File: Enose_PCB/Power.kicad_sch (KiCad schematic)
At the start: 53 parts, among them IC1 ISL91127IRNZ-T7A, J5 USB_C_Receptacle_USB2.0_16P, J6 Battery Terminal, SW3 SW_DPST_x2, U2 USBLC6-2P6, U3 MP2721GRH-0000-P

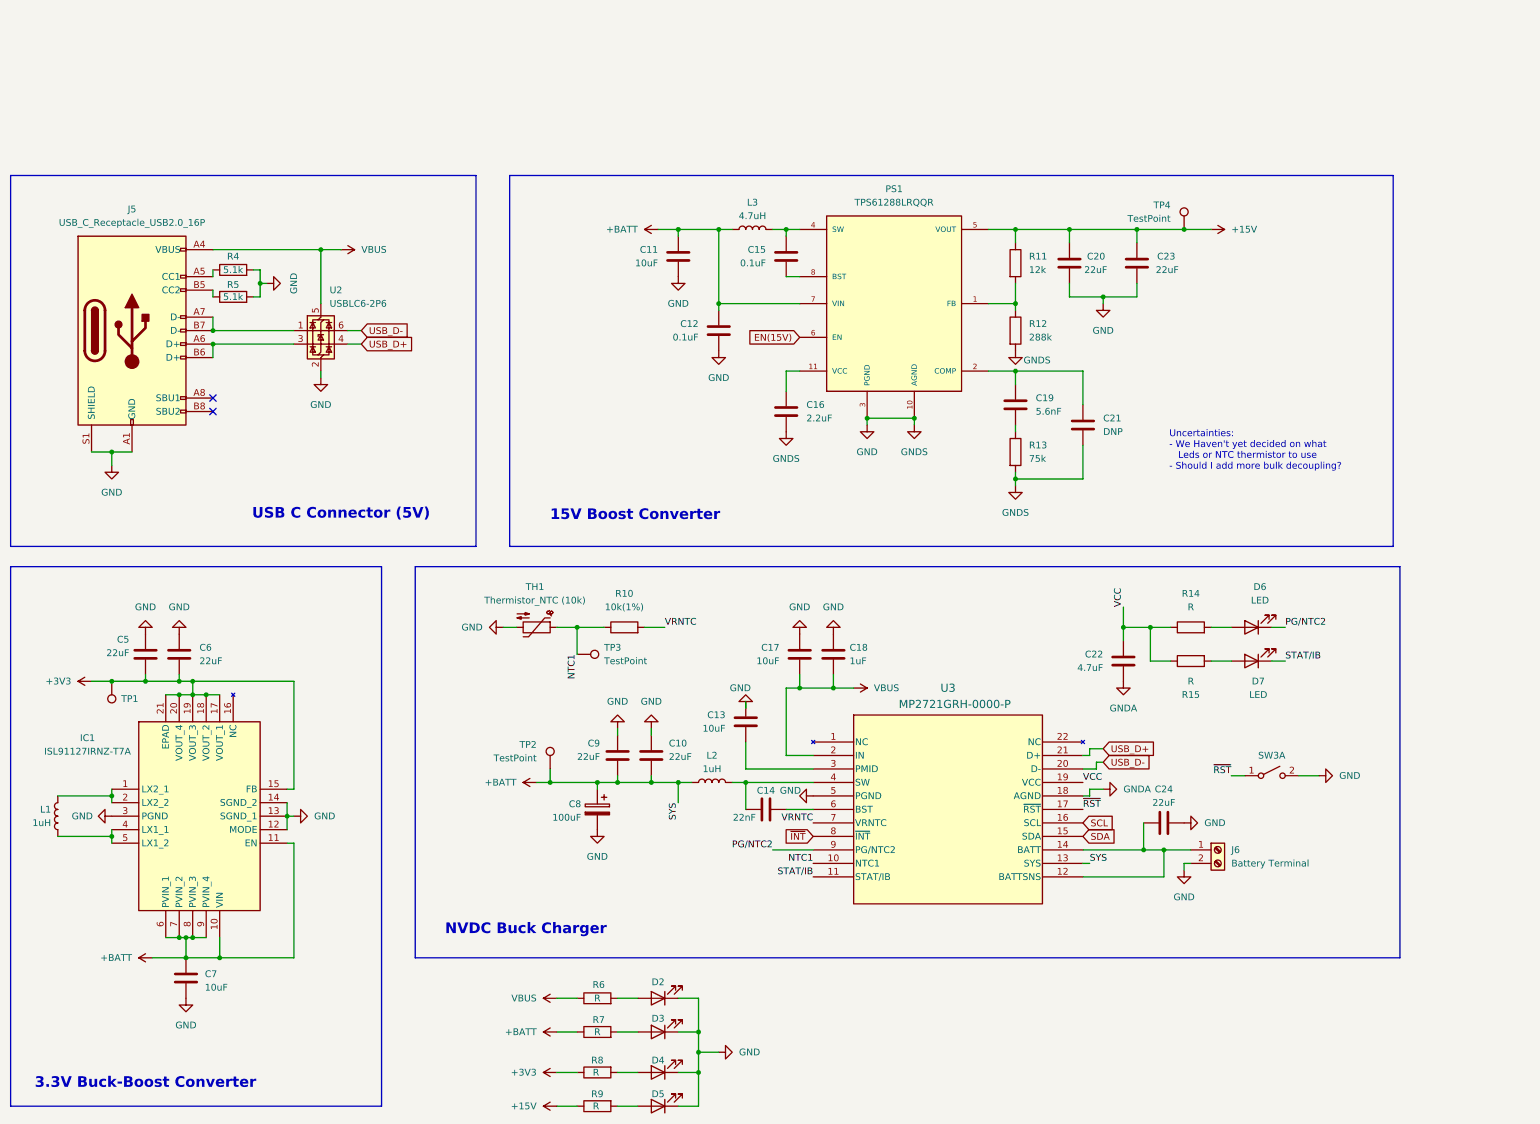
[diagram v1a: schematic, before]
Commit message: Added LED
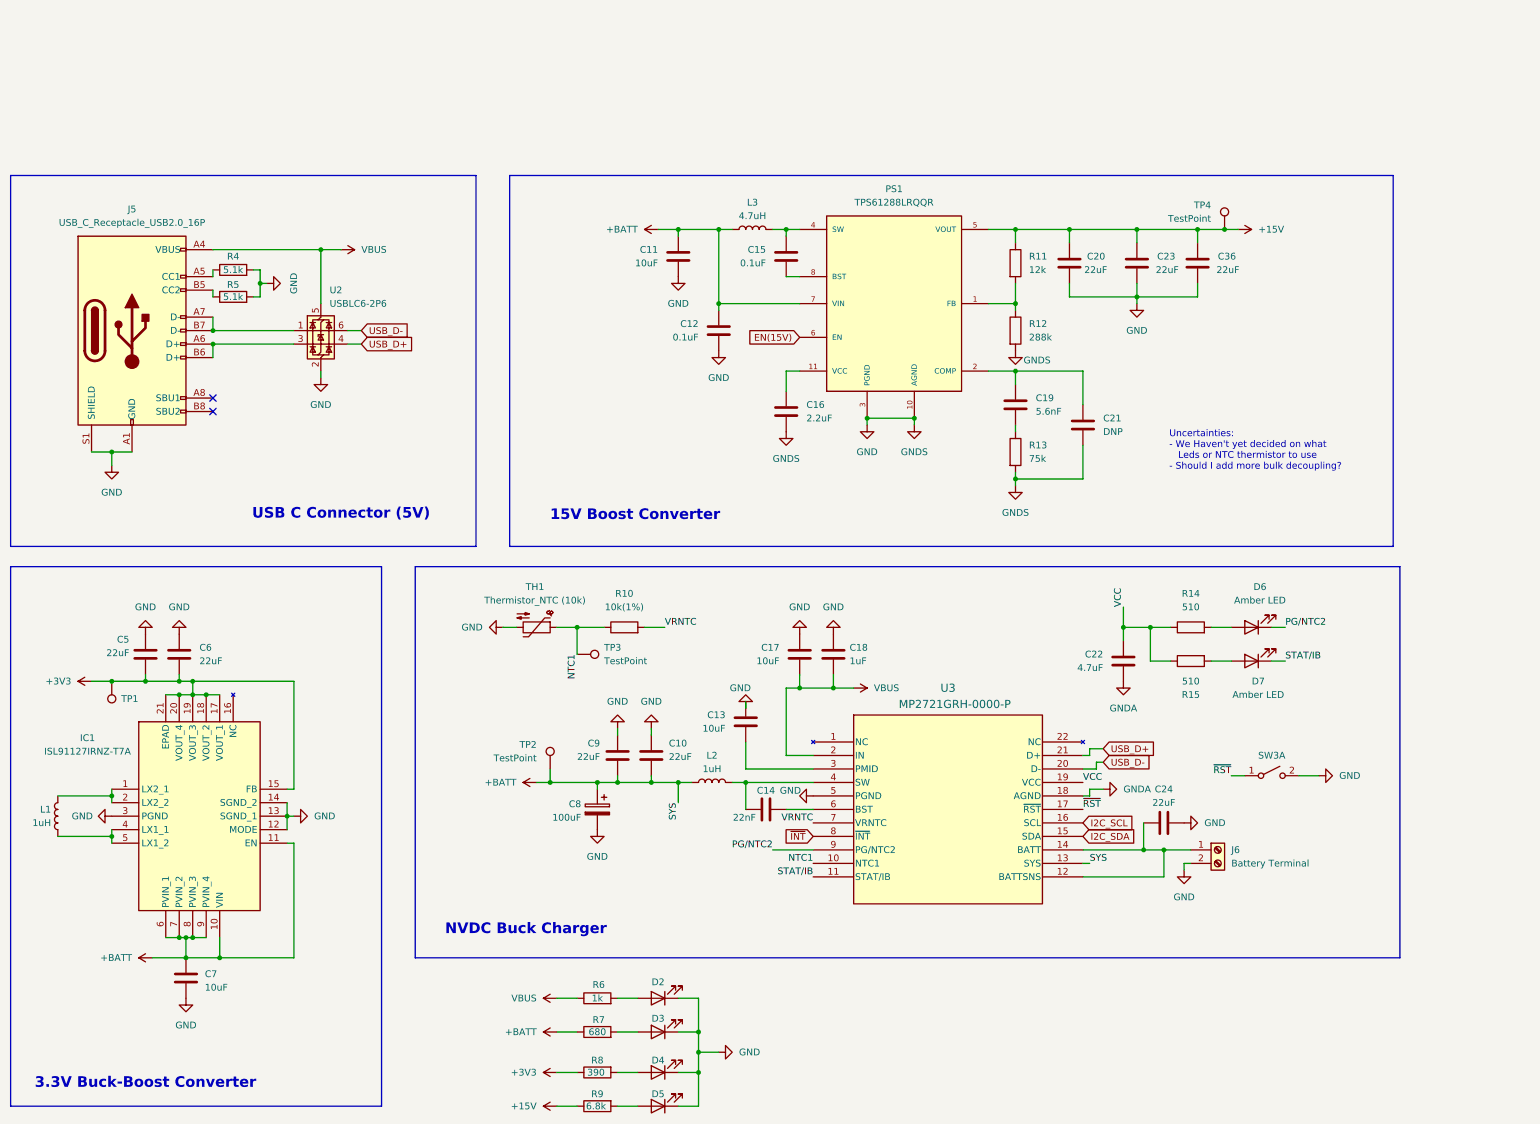
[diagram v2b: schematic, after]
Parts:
- added C36: 22uF, Capacitor_THT:C_Disc_D6.0mm_W4.4mm_P5.00mm, symbol Device:C
- C20, C23: footprint (none) -> Capacitor_SMD:C_1210_3225Metric
- D4, D5: value LED -> LED GREEN
- D6, D7: value LED -> Amber LED
- R14, R15: value R -> 510
- R6: value R -> 1k
- R7: value R -> 680
- R8: value R -> 390
- R9: value R -> 6.8k
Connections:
- net +15V: now also C36.1
- net GND: now also C36.2
- net SCL renamed I2C_SCL
- net SDA renamed I2C_SDA
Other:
- moved on the sheet: TP4
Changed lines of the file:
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@@
 	)
 	(junction
+		(at 248.92 25.4)
+		(diameter 0)
+		(color 0 0 0 0)
+	)
+	(junction
 		(at 149.86 180.34)
 		(diameter 0)
@@
 	)
 	(junction
+		(at 232.41 38.1)
+		(diameter 0)
+		(color 0 0 0 0)
+	)
+	(junction
 		(at 229.87 100.33)
 		(diameter 0)
@@
 	)
 	(junction
-		(at 241.3 25.4)
-		(diameter 0)
-		(color 0 0 0 0)
-	)
-	(junction
 		(at 67.31 35.56)
 		(diameter 0)
@@
 	)
 	(junction
+		(at 243.84 25.4)
+		(diameter 0)
+		(color 0 0 0 0)
+	)
+	(junction
 		(at 209.55 72.39)
 		(diameter 0)
@@
 	)
 	(junction
-		(at 226.06 38.1)
-		(diameter 0)
-		(color 0 0 0 0)
-	)
-	(junction
 		(at 58.42 44.45)
 		(diameter 0)
@@
 	(wire
 		(pts
+			(xy 243.84 25.4) (xy 243.84 27.94)
+		)
+		(stroke
+			(width 0)
+			(type default)
+		)
+	)
+	(wire
+		(pts
 			(xy 58.42 29.21) (xy 78.74 29.21)
 		)
@@
 	(wire
 		(pts
-			(xy 232.41 25.4) (xy 241.3 25.4)
+			(xy 232.41 25.4) (xy 243.84 25.4)
 		)
 		(stroke
@@
 	(wire
 		(pts
-			(xy 219.71 38.1) (xy 226.06 38.1)
+			(xy 219.71 38.1) (xy 232.41 38.1)
 		)
 		(stroke
@@
 	(wire
 		(pts
-			(xy 241.3 25.4) (xy 246.38 25.4)
-		)
-		(stroke
-			(width 0)
-			(type default)
-		)
-	)
-	(wire
-		(pts
 			(xy 123.19 170.18) (xy 127 170.18)
 		)
@@
 	(wire
 		(pts
-			(xy 226.06 38.1) (xy 232.41 38.1)
-		)
-		(stroke
-			(width 0)
-			(type default)
-		)
-	)
-	(wire
-		(pts
 			(xy 262.89 128.27) (xy 266.7 128.27)
 		)
@@
 	(wire
 		(pts
-			(xy 226.06 38.1) (xy 226.06 39.37)
+			(xy 232.41 38.1) (xy 232.41 39.37)
 		)
 		(stroke
@@
 	(wire
 		(pts
+			(xy 243.84 38.1) (xy 232.41 38.1)
+		)
+		(stroke
+			(width 0)
+			(type default)
+		)
+	)
+	(wire
+		(pts
 			(xy 229.87 100.33) (xy 234.95 100.33)
 		)
@@
 	(wire
 		(pts
+			(xy 243.84 35.56) (xy 243.84 38.1)
+		)
+		(stroke
+			(width 0)
+			(type default)
+		)
+	)
+	(wire
+		(pts
 			(xy 123.19 176.53) (xy 127 176.53)
 		)
@@
 	(wire
 		(pts
+			(xy 243.84 25.4) (xy 248.92 25.4)
+		)
+		(stroke
+			(width 0)
+			(type default)
+		)
+	)
+	(wire
+		(pts
 			(xy 222.25 147.32) (xy 237.49 147.32)
 		)
@@
 	(wire
 		(pts
+			(xy 248.92 25.4) (xy 251.46 25.4)
+		)
+		(stroke
+			(width 0)
+			(type default)
+		)
+	)
+	(wire
+		(pts
 			(xy 223.52 132.08) (xy 222.25 132.08)
 		)
@@
 		)
 	)
-	(global_label "SDA"
+	(global_label "I2C_SDA"
 		(shape input)
 		(at 222.25 139.7 0)
@@
 		)
 		(property "Intersheetrefs" "${INTERSHEET_REFS}"
-			(at 228.8033 139.7 0)
+			(at 232.8552 139.7 0)
 			(effects
 				(font
@@
 		)
 	)
-	(global_label "SCL"
+	(global_label "I2C_SCL"
 		(shape input)
 		(at 222.25 137.16 0)
@@
 		)
 		(property "Intersheetrefs" "${INTERSHEET_REFS}"
-			(at 228.7428 137.16 0)
+			(at 232.7947 137.16 0)
 			(effects
 				(font
@@
 			)
 		)
-		(property "Value" "LED"
+		(property "Value" "Amber LED"
 			(at 255.27 113.03 0)
 			(effects
@@
 			)
 		)
-		(property "Value" "R"
+		(property "Value" "1k"
 			(at 130.81 170.18 90)
 			(effects
@@
 			)
 		)
-		(property "Value" "LED"
+		(property "Value" "Amber LED"
 			(at 255.5875 95.25 0)
 			(effects
@@
 			)
 		)
-		(property "Value" "LED"
+		(property "Value" "LED GREEN"
 			(at 143.764 189.738 0)
 			(effects
@@
 			)
 		)
-		(property "Footprint" ""
+		(property "Footprint" "Capacitor_SMD:C_1210_3225Metric"
 			(at 220.6752 35.56 0)
 			(effects
@@
 	(symbol
 		(lib_id "power:+15V")
-		(at 246.38 25.4 270)
+		(at 251.46 25.4 270)
 		(unit 1)
 		(exclude_from_sim no)
@@
 		(fields_autoplaced yes)
 		(property "Reference" "#PWR031"
-			(at 242.57 25.4 0)
+			(at 247.65 25.4 0)
 			(effects
 				(font
@@
 		)
 		(property "Value" "+15V"
-			(at 250.19 25.3999 90)
+			(at 255.27 25.3999 90)
 			(effects
 				(font
@@
 		)
 		(property "Footprint" ""
-			(at 246.38 25.4 0)
+			(at 251.46 25.4 0)
 			(effects
 				(font
@@
 		)
 		(property "Datasheet" ""
-			(at 246.38 25.4 0)
+			(at 251.46 25.4 0)
 			(effects
 				(font
@@
 		)
 		(property "Description" "Power symbol creates a global label with name \"+15V\""
-			(at 246.38 25.4 0)
+			(at 251.46 25.4 0)
 			(effects
 				(font
@@
 			)
 		)
-		(property "Value" "R"
+		(property "Value" "390"
 			(at 130.556 184.15 90)
 			(effects
@@
 			)
 		)
-		(property "Value" "R"
+		(property "Value" "510"
 			(at 242.57 96.52 90)
 			(effects
@@
 			)
 		)
-		(property "Value" "LED"
+		(property "Value" "LED GREEN"
 			(at 143.764 196.088 0)
 			(effects
@@
 			)
 		)
-		(property "Value" "R"
+		(property "Value" "6.8k"
 			(at 130.556 190.5 90)
 			(effects
@@
 			)
 		)
-		(property "Value" "R"
+		(property "Value" "510"
 			(at 242.57 110.49 90)
 			(effects
@@
 			)
 		)
-		(property "Value" "R"
+		(property "Value" "680"
 			(at 130.81 176.53 90)
 			(effects
@@
 	)
 	(symbol
+		(lib_id "Device:C")
+		(at 243.84 31.75 0)
+		(unit 1)
+		(exclude_from_sim no)
+		(in_bom yes)
+		(on_board yes)
+		(dnp no)
+		(property "Reference" "C36"
+			(at 247.65 30.4799 0)
+			(effects
+				(font
+					(size 1.27 1.27)
+				)
+				(justify left)
+			)
+		)
+		(property "Value" "22uF"
+			(at 247.396 33.02 0)
+			(effects
+				(font
+					(size 1.27 1.27)
+				)
+				(justify left)
+			)
+		)
+		(property "Footprint" "Capacitor_THT:C_Disc_D6.0mm_W4.4mm_P5.00mm"
+			(at 244.8052 35.56 0)
+			(effects
+				(font
+					(size 1.27 1.27)
+				)
+				(hide yes)
+			)
+		)
+		(property "Datasheet" "~"
+			(at 243.84 31.75 0)
+			(effects
+				(font
+					(size 1.27 1.27)
+				)
+				(hide yes)
+			)
+		)
+		(property "Description" "Unpolarized capacitor"
+			(at 243.84 31.75 0)
+			(effects
+				(font
+					(size 1.27 1.27)
+				)
+				(hide yes)
+			)
+		)
+		(pin "2"
+		)
+		(pin "1"
+		)
+		(instances
+			(project "Enose_PCB"
+				(path "/eef70be0-4107-491c-8ca0-465071a6397e/c704ca63-8ab0-46ce-942e-504221cfea41"
+					(reference "C36")
+					(unit 1)
+				)
+			)
+		)
+	)
+	(symbol
 		(lib_id "Device:R")
 		(at 209.55 44.45 0)
@@
 	(symbol
 		(lib_id "power:GND")
-		(at 226.06 39.37 0)
+		(at 232.41 39.37 0)
 		(unit 1)
 		(exclude_from_sim no)
@@
 		(fields_autoplaced yes)
 		(property "Reference" "#PWR029"
-			(at 226.06 45.72 0)
+			(at 232.41 45.72 0)
 			(effects
 				(font
@@
 		)
 		(property "Value" "GND"
-			(at 226.06 44.45 0)
+			(at 232.41 44.45 0)
 			(effects
 				(font
@@
 		)
 		(property "Footprint" ""
-			(at 226.06 39.37 0)
+			(at 232.41 39.37 0)
 			(effects
 				(font
@@
 		)
 		(property "Datasheet" ""
-			(at 226.06 39.37 0)
+			(at 232.41 39.37 0)
 			(effects
 				(font
@@
 		)
 		(property "Description" "Power symbol creates a global label with name \"GND\" , ground"
-			(at 226.06 39.37 0)
+			(at 232.41 39.37 0)
 			(effects
 				(font
@@
 	(symbol
 		(lib_id "Connector:TestPoint")
-		(at 241.3 25.4 0)
+		(at 248.92 25.4 0)
 		(mirror y)
 		(unit 1)
@@
 		(dnp no)
 		(property "Reference" "TP4"
-			(at 238.76 20.8279 0)
+			(at 246.38 20.8279 0)
 			(effects
 				(font
@@
 		)
 		(property "Value" "TestPoint"
-			(at 238.76 23.3679 0)
+			(at 246.38 23.3679 0)
 			(effects
 				(font
@@
 		)
 		(property "Footprint" ""
-			(at 236.22 25.4 0)
+			(at 243.84 25.4 0)
 			(effects
 				(font
@@
 		)
 		(property "Datasheet" "~"
-			(at 236.22 25.4 0)
+			(at 243.84 25.4 0)
 			(effects
 				(font
@@
 		)
 		(property "Description" "test point"
-			(at 241.3 25.4 0)
+			(at 248.92 25.4 0)
 			(effects
 				(font
@@
 			)
 		)
-		(property "Footprint" ""
+		(property "Footprint" "Capacitor_SMD:C_1210_3225Metric"
 			(at 233.3752 35.56 0)
 			(effects

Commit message: Changed Battery Charger
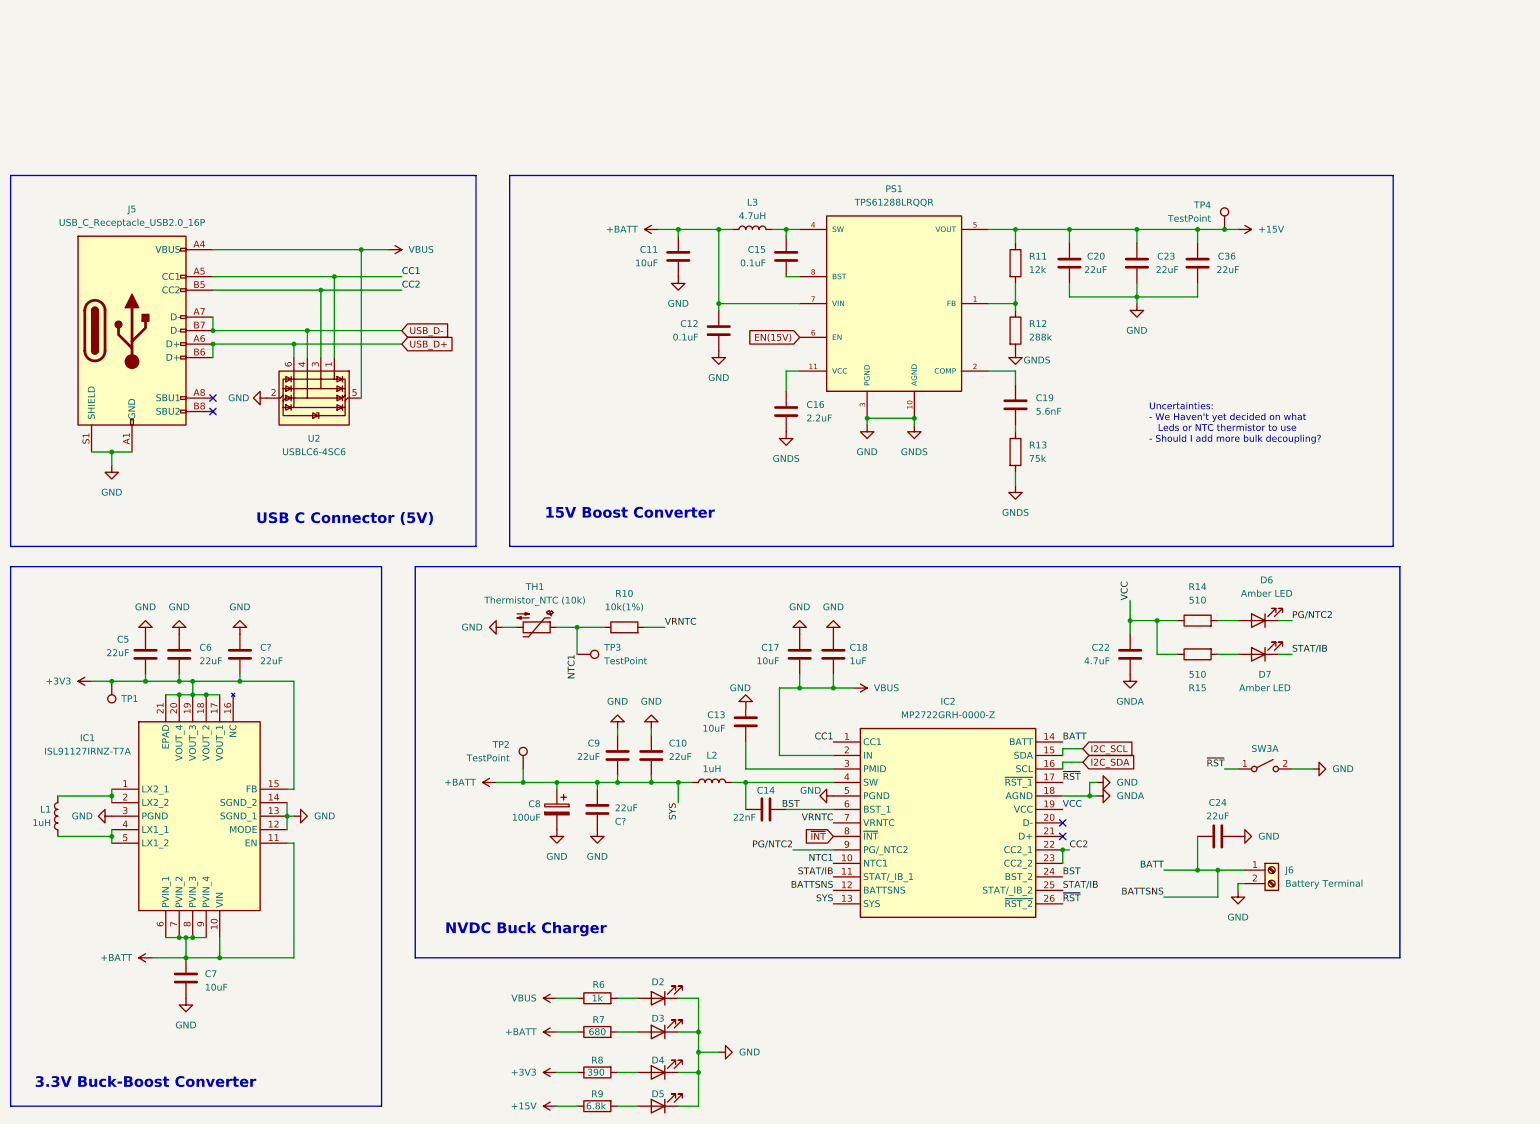
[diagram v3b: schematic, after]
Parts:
- removed C21: DNP, symbol Device:C
- removed R4, R5: 5.1k, symbol Device:R
- removed U2: USBLC6-2P6, Package_TO_SOT_SMD:SOT-666, symbol Power_Protection:USBLC6-2P6
- removed U3: MP2721GRH-0000-P, QFN-22_MP2721_MNP, symbol MP2721GRH-0000-P:MP2721GRH-0000-P
- added C? (x2): 22uF, symbol Device:C
- added IC2: MP2722GRH-0000-Z, MP2722GRH0000Z, symbol SamacSys_Parts:MP2722GRH-0000-Z
- added U2: USBLC6-4SC6, Package_TO_SOT_SMD:SOT-23-6, symbol Power_Protection:USBLC6-4SC6
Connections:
- net GNDA is gone; now on net GND: C22.2
- net +3V3: now also C?.2
- net +BATT: now also C?.1, IC2.13 (SYS)
- net GND: now also C?.1, C?.2, IC2.18 (AGND), IC2.5 (PGND), U2.2 (GND)
- net I2C_SCL: now also IC2.15 (SDA)
- net I2C_SDA: now also IC2.16 (SCL)
- net NTC1: now also IC2.10 (NTC1)
- net PG/NTC2: now also IC2.9 (PG/_NTC2)
- net STAT/IB: now also IC2.11 (STAT/_IB_1), IC2.25 (STAT/_IB_2)
- net USB_D+: now also J5.A6 (D+), J5.B6 (D+), U2.6 (I/O4)
- net USB_D-: now also J5.A7 (D-), J5.B7 (D-), U2.4 (I/O3)
- net VBUS: now also IC2.2 (IN), U2.5 (VBUS)
- net VCC: now also IC2.19 (VCC)
- net VRNTC: now also IC2.7 (VRNTC)
- net ~{INT}: now also IC2.8 (~{INT})
- net ~{RST}: now also IC2.17 (~{RST_1}), IC2.26 (~{RST_2})
- net at C14.1, L2.2: now also IC2.4 (SW)
- net CC2: now reaches J5.B5 (CC2)
- net CC2: now also IC2.22 (CC2_1), IC2.23 (CC2_2), U2.3 (I/O2)
- net BATT: now reaches C24.2, J6.1 (Pin_1)
- net BATT: now also IC2.12 (BATTSNS), IC2.14 (BATT)
- net at C13.1: now also IC2.3 (PMID)
- net BST: now reaches C14.2
- net BST: now also IC2.24 (BST_2), IC2.6 (BST_1)
- net CC1: now reaches J5.A5 (CC1)
- net CC1: now also IC2.1 (CC1), U2.1 (I/O1)
- no-connect marks 2 -> 4
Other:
- moved on the sheet: C22, C24, C8, D6, D7, J6, R14, R15, SW3A, TP2
